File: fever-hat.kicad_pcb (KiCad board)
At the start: 2 copper layers, 65.5 x 56.5 mm, 36 parts, among them IC1 MPM3630GQV-P, IC2 TPS2540RTET, J1 Raspberry_Pi_2_3, J2 Thermal Camera, J3 USB_B, J4 USB_A, J5 Conn_01x04, J6 Barrel_Jack_Switch, Q1 Q_NMOS_GSD, Q2 Q_PMOS_DGS

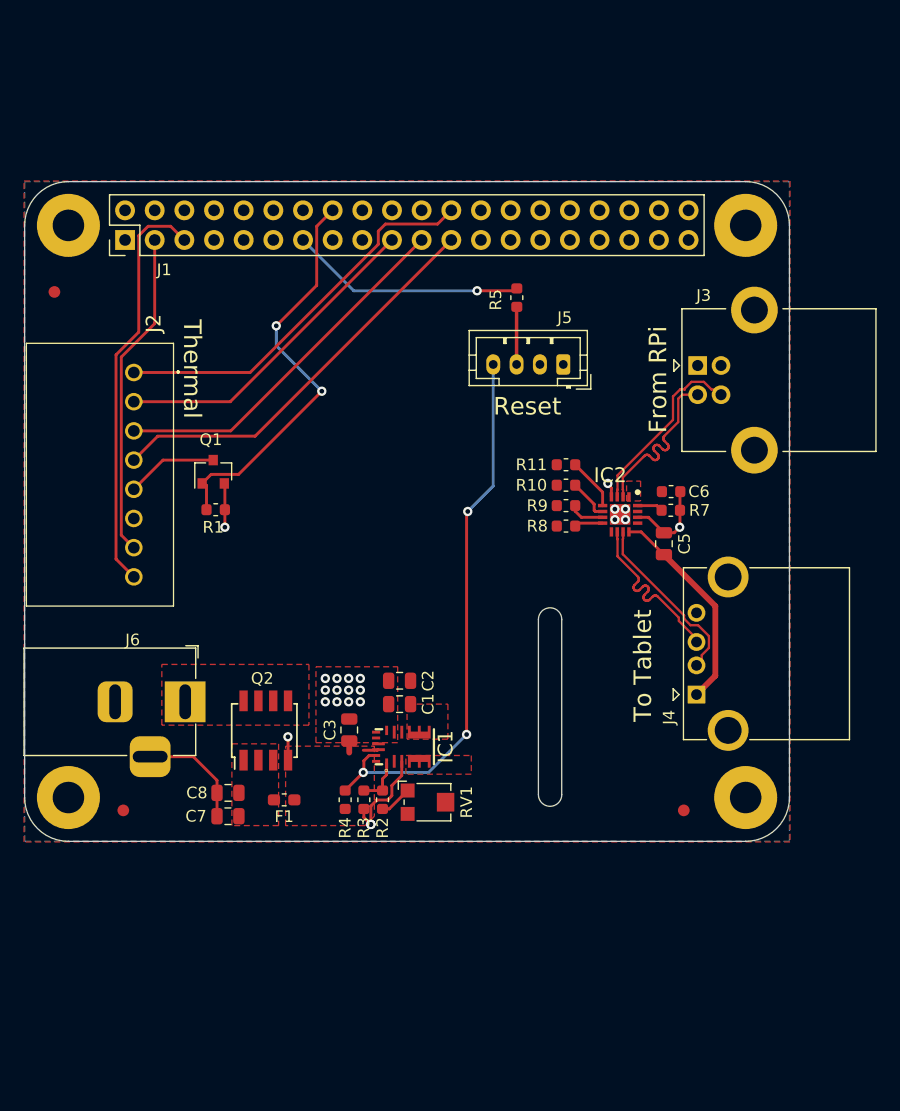
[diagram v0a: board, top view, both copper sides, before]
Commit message: Smaller PCB and use buck converter that JLCPCB can provide
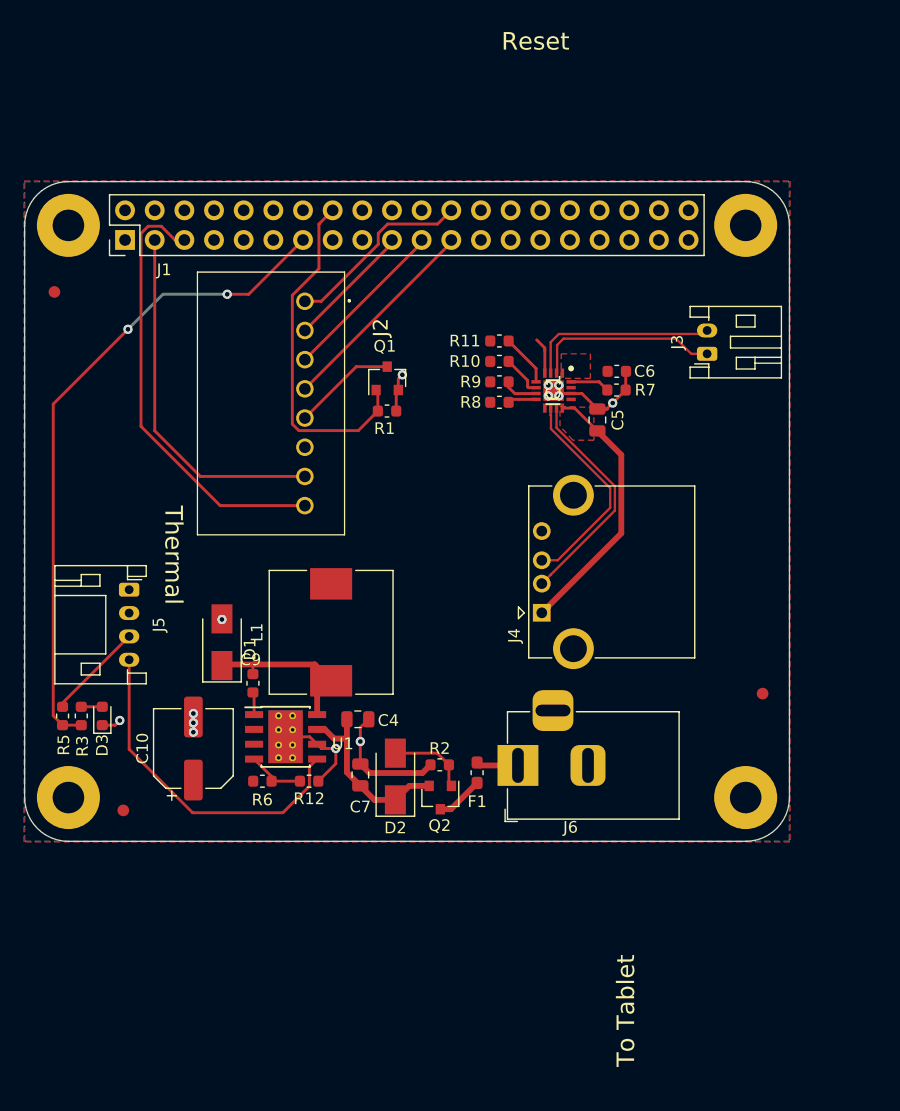
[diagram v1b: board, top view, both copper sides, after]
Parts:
- removed C1, C2, C3, C8: 22uF, Capacitor_SMD:C_0805_2012Metric
- removed IC2: TPS2540RTET, TPS2540RTET:QFN50P300X300X80-17N-D
- removed R4: 100K, Resistor_SMD:R_0603_1608Metric
- removed RV1: R_POT_TRIM, Potentiometer_SMD:Potentiometer_Bourns_TC33X_Vertical
- added C10: 220uF, Capacitor_SMD:CP_Elec_6.3x7.7, F.Cu at (110.7, 144.8)
- added C4: 10uF, Capacitor_SMD:C_0805_2012Metric, F.Cu at (124.8, 142.3)
- added C9: 0.01uF, Capacitor_SMD:C_0603_1608Metric, F.Cu at (115.8, 139.2)
- added D1: B340A, Diode_SMD:D_SMA, F.Cu at (113.2, 135.7)
- added D2: D_Zener, Diode_SMD:D_SMA, F.Cu at (128.0, 147.2)
- added D3: LED, Diode_SMD:D_0603_1608Metric, F.Cu at (102.9, 142.0)
- added L1: 15uH, Inductor_SMD:L_10.4x10.4_H4.8, F.Cu at (122.5, 134.8)
- added R12: 3K16, Resistor_SMD:R_0603_1608Metric, F.Cu at (120.6, 147.6)
- added R6: 10K, Resistor_SMD:R_0603_1608Metric, F.Cu at (116.6, 147.6)
- added U1: TPS5430DDA, Package_SO:TI_SO-PowerPAD-8_ThermalVias, F.Cu at (118.6, 143.8)
- IC1: value MPM3630GQV-P -> TPS2546RTER; footprint MPM3630GQV-P:QFN-20(3MMX5MMX1.6MM) -> QFN50P300X300X80-17N-D
- J3: value USB_B -> Conn_01x02; footprint Connector_USB:USB_B_Lumberg_2411_02_Horizontal -> Connector_JST:JST_PH_S2B-PH-K_1x02_P2.00mm_Horizontal
- J5: footprint Connector_JST:JST_PH_B4B-PH-K_1x04_P2.00mm_Vertical -> Connector_JST:JST_PH_S4B-PH-K_1x04_P2.00mm_Horizontal
- Q2: value Q_PMOS_DGS -> Q_PMOS_GDS; footprint footprints:IRF9310PbF -> Package_TO_SOT_SMD:SOT-23
- R2: value 51K -> 100K
- R3: value 6K98 -> 470R
- R7: value 39K -> 36K
- moved R5 52.9 mm to (99.5, 142.0), turned to 90 degrees
- moved J5 41.9 mm to (105.2, 131.2), turned to 270 degrees
- moved IC1 33.1 mm to (141.6, 114.2), turned to 270 degrees
- moved J6 29.0 mm to (138.5, 146.2), turned to 180 degrees
- moved R3 25.2 mm to (101.1, 142.0), turned to 90 degrees
- moved Q2 17.2 mm to (131.8, 149.0), turned to 270 degrees
- moved R1 16.9 mm to (127.3, 115.9)
- moved Q1 16.9 mm to (127.3, 113.1)
- moved F1 16.7 mm to (135.0, 146.9), turned to 90 degrees
- moved J2 15.9 mm to (120.2, 106.5)
- moved J4 15.0 mm to (140.5, 133.2)
- moved FID3 12.1 mm to (159.4, 140.1)
- moved R10 12.0 mm to (136.9, 111.7)
- moved R11 12.0 mm to (136.9, 109.9)
- moved R8 12.0 mm to (136.9, 115.2)
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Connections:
- C7 pad 1: Net-(C7-Pad1) -> VCC
- F1 pad 1: VCC -> Net-(F1-Pad1)
- F1 pad 2: Net-(C7-Pad1) -> Net-(F1-Pad2)
- IC1 pad 1: Net-(IC1-Pad1) -> +5V
- IC1 pad 10: Net-(IC1-Pad10) -> /D_IN_P
- IC1 pad 11: Net-(IC1-Pad11) -> /D_IN_N
- IC1 pad 12: GND -> Net-(C5-Pad1)
- IC1 pad 13: GND -> Net-(IC1-Pad13)
- IC1 pad 16: VCC -> Net-(IC1-Pad16)
- IC1 pad 17: /RESET -> GND
- IC1 pad 2: Net-(IC1-Pad2) -> /D_OUT_N
- IC1 pad 3: GND -> /D_OUT_P
- IC1 pad 4: Net-(IC1-Pad4) -> +5V
- IC1 pad 5: Net-(IC1-Pad4) -> Net-(IC1-Pad5)
- IC1 pad 6: Net-(IC1-Pad4) -> Net-(IC1-Pad6)
- IC1 pad 7: +5V -> Net-(IC1-Pad7)
- IC1 pad 8: +5V -> Net-(IC1-Pad8)
- IC1 pad 9: +5V -> Net-(IC1-Pad9)
- J3 pad 1: Net-(J3-Pad1) -> /D_OUT_N
- J3 pad 2: /D_OUT_N -> /D_OUT_P
- J6 pad 1: Net-(J6-Pad1) -> Net-(F1-Pad2)
- Q2 pad 1: Net-(J6-Pad1) -> Net-(D2-Pad2)
- Q2 pad 2: GND -> VCC
- Q2 pad 3: Net-(C7-Pad1) -> Net-(F1-Pad1)
- R10 pad 2: Net-(IC2-Pad6) -> Net-(IC1-Pad6)
- R11 pad 2: Net-(IC2-Pad5) -> Net-(IC1-Pad5)
- R2 pad 1: Net-(R2-Pad1) -> Net-(D2-Pad2)
- R2 pad 2: Net-(IC1-Pad1) -> GND
- R3 pad 1: Net-(IC1-Pad1) -> /LED_INDICATOR
- R3 pad 2: GND -> Net-(D3-Pad2)
- R7 pad 2: Net-(IC2-Pad16) -> Net-(IC1-Pad16)
- R8 pad 2: Net-(IC2-Pad8) -> Net-(IC1-Pad8)
- R9 pad 2: Net-(IC2-Pad7) -> Net-(IC1-Pad7)
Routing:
- net /LED_INDICATOR: track 20.2 -> 56.6 mm, vias 1 -> 2
- net /RESET: track 47.3 -> 28.9 mm, vias 3 -> 0
- net /SPI_CEO: track 33.6 -> 16.3 mm
- net /SPI_SCLK: track 35.0 -> 17.9 mm
- net /SPI_MISO: track 31.4 -> 14.4 mm
- net /SPI_MOSI: track 27.8 -> 10.8 mm
- net Net-(C9-Pad1): track 0.00 -> 14.3 mm
- net VCC: track 2.32 -> 15.9 mm
- net Net-(D2-Pad2): track 0.00 -> 6.89 mm
- net /THERMAL_POWER: track 35.0 -> 29.8 mm, vias 2 -> 0
- net Net-(R12-Pad1): track 0.00 -> 4.94 mm
- net Net-(C5-Pad1): track 18.3 -> 23.1 mm
- net Net-(IC1-Pad5): track 0.00 -> 4.47 mm
- net Net-(IC2-Pad5): track 4.47 -> 0.00 mm
- net /D_IN_N: track 15.3 -> 19.7 mm
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- added copper zone on F.Cu, net Net-(C5-Pad1)
- removed copper zone on F.Cu, net GND
- removed copper zone on F.Cu, net Net-(C7-Pad1)
- removed copper zone on F.Cu, net Net-(IC1-Pad4)
- removed copper zone on F.Cu, net Net-(J6-Pad1)
- removed copper zone on F.Cu, net VCC
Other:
- outline, holes or cut-outs redrawn
- board text removed: "From RPi"

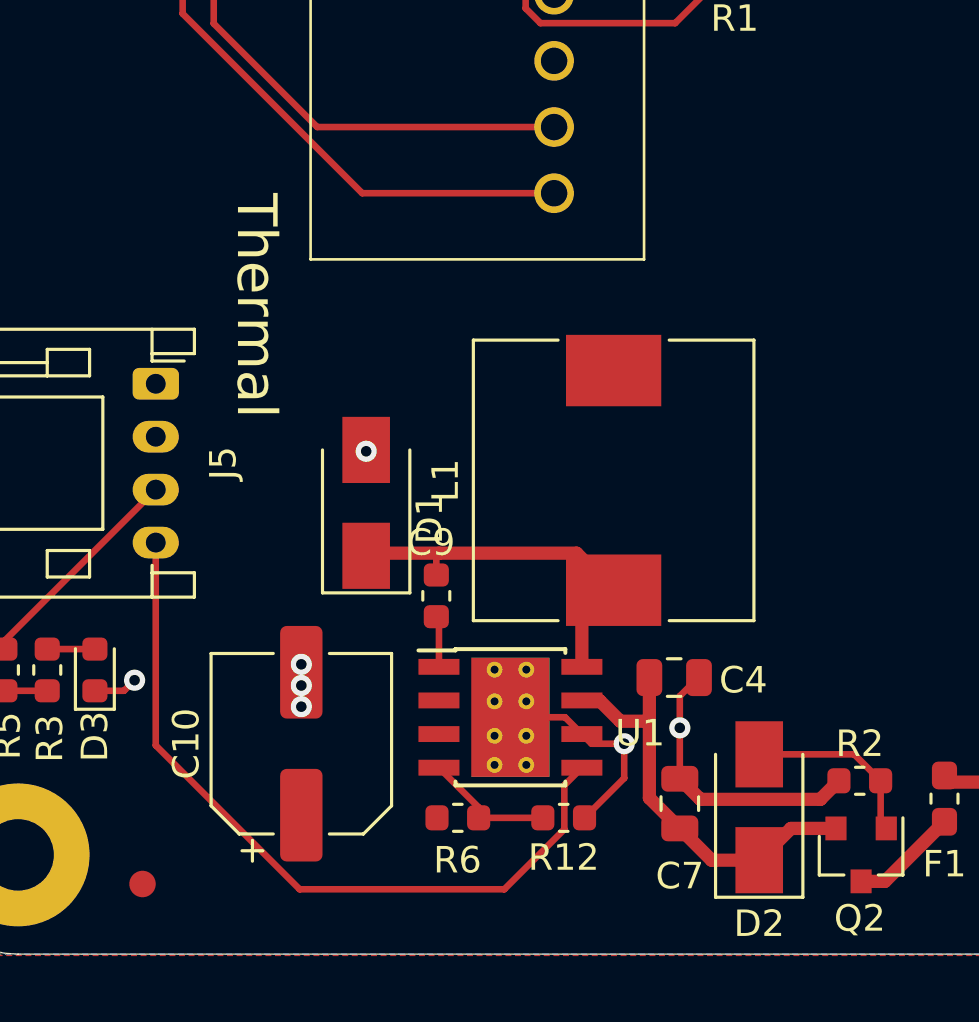
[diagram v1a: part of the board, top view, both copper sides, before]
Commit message: Update unductor footprint
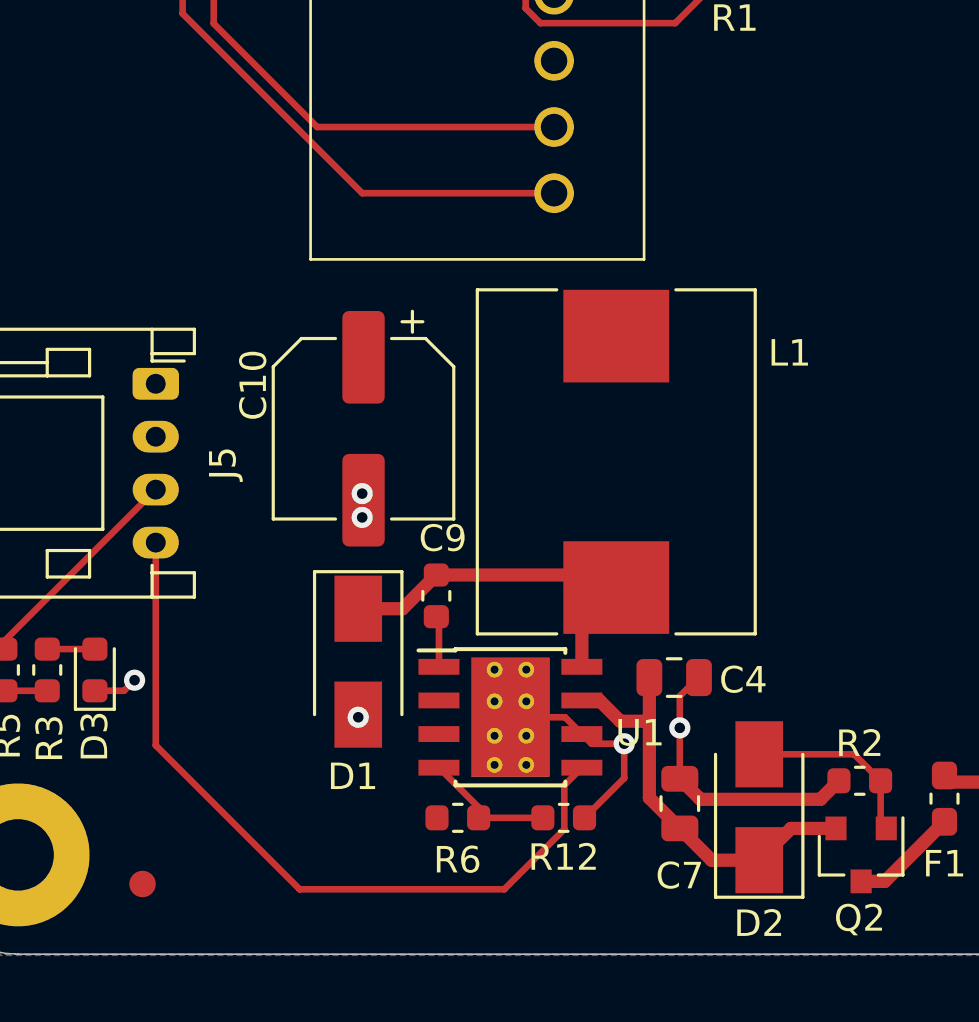
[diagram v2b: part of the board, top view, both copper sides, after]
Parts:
- L1: footprint Inductor_SMD:L_10.4x10.4_H4.8 -> footprints:MWSA1004-150MT
- moved C10 12.1 mm to (113.0, 132.9), turned to 270 degrees
- moved D1 6.01 mm to (112.8, 141.7), turned to 270 degrees
- moved L1 0.71 mm to (122.6, 134.2)
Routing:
- net Net-(C9-Pad1): track 14.3 -> 13.8 mm
- net GND: vias 13 -> 12
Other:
- board text removed: "Thermal"
